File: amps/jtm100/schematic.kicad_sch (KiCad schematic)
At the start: 82 parts, among them T1 OT

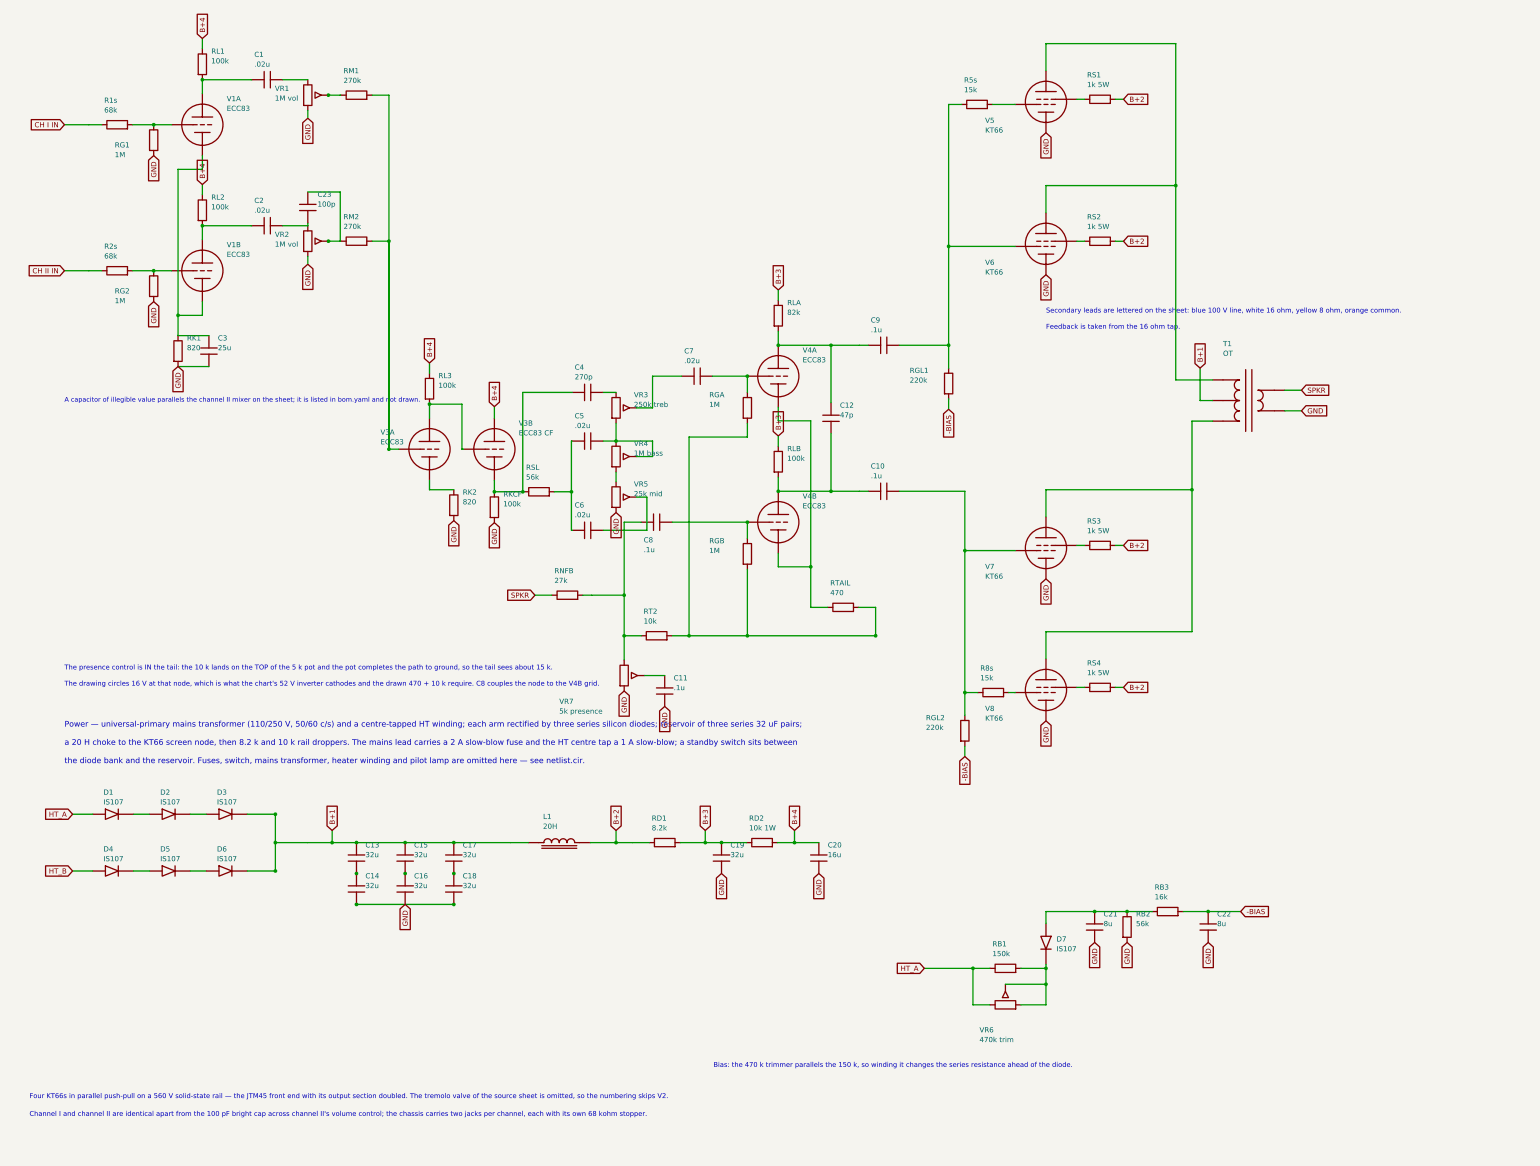
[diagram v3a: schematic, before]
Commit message: Fix: deterministic schematic ids and wires split at every join
- _u() is uuid5 over (amp id, emission order), so a regeneration of an
  unchanged script is byte-identical and a drift gate becomes possible
- write() splits wire segments at symbol pins, wire ends and junction dots,
  so the file connects exactly what the drawing shows under KiCad's
  endpoint-only semantics (270 pins were on a wire's interior; net
  partitions unchanged on all 38 sheets)
- all sheets regenerated; aa864-bassman title block was stale (draft) and
  now matches meta.yaml (verified)

Co-Authored-By: Claude Fable 5.1 <noreply@anthropic.com>
Claude-Session: https://claude.ai/code/session_01KBMfdh37HmCL2iWcBiL5J1
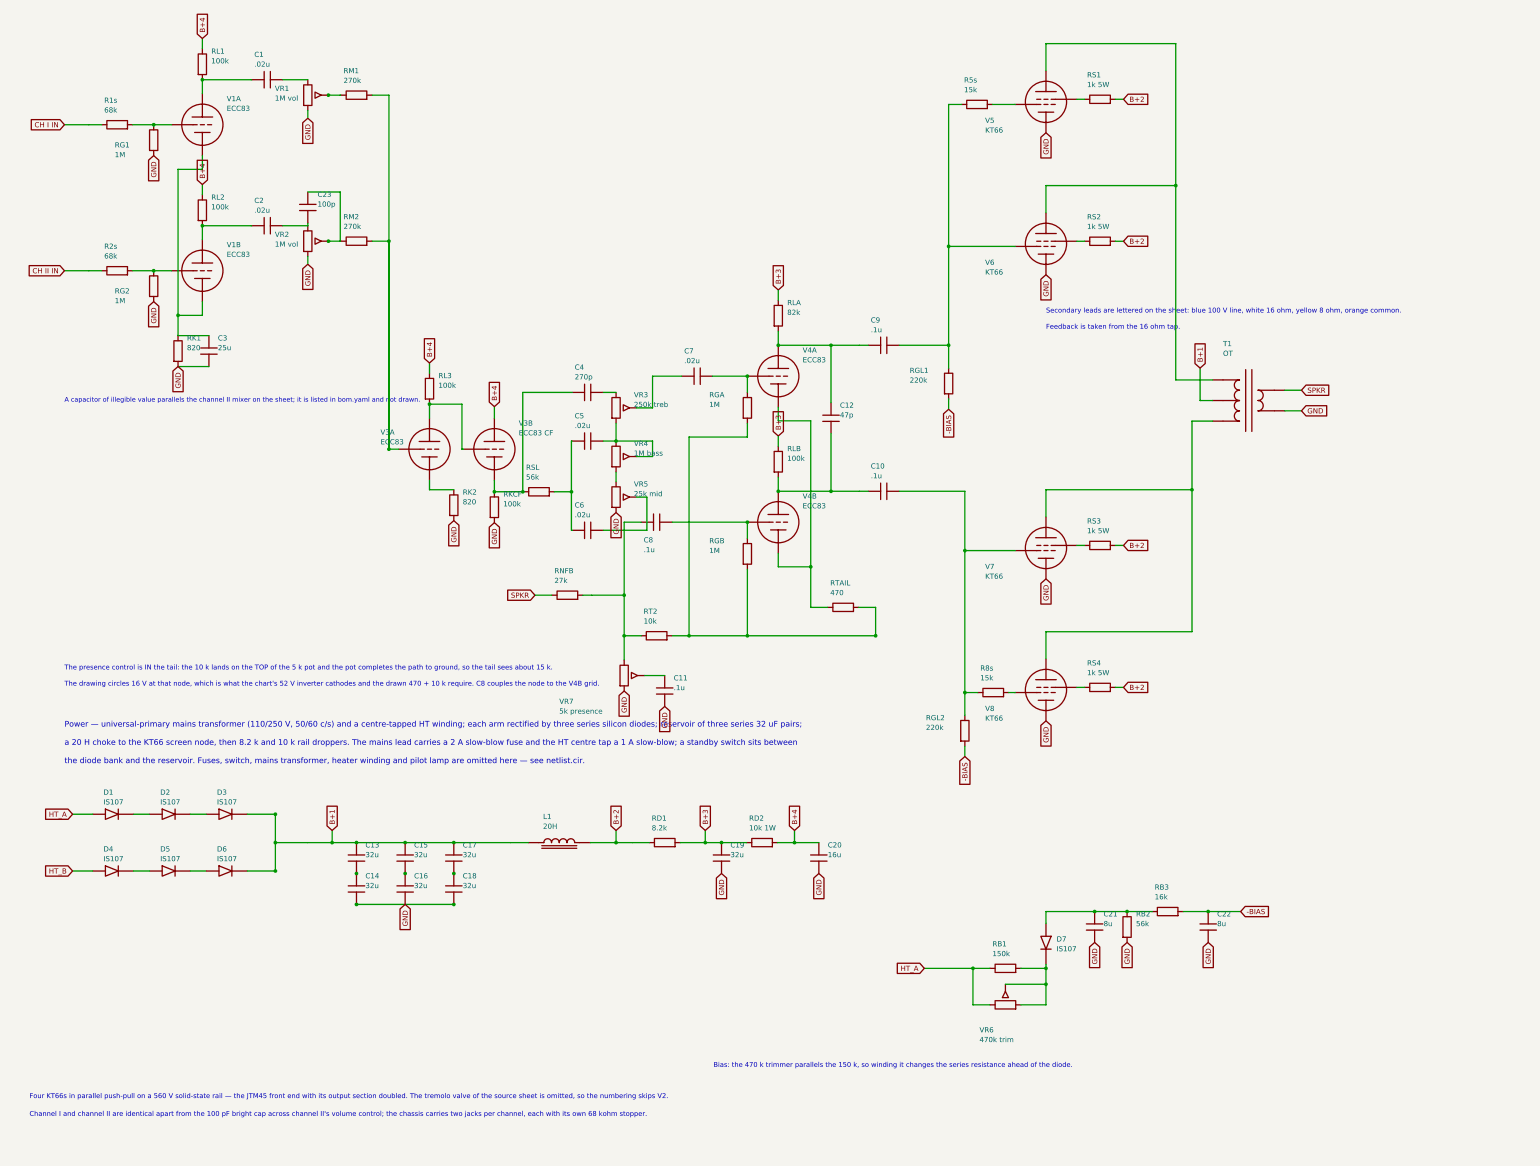
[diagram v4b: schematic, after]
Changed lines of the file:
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@@
   (wire (pts (xy 27.336 38.278) (xy 30.526 38.278))
     (stroke (width 0) (type default)))
-  (wire (pts (xy 38.146 38.278) (xy 47.716 38.278))
+  (wire (pts (xy 38.146 38.278) (xy 43.336 38.278))
+    (stroke (width 0) (type default)))
+  (wire (pts (xy 43.336 38.278) (xy 47.716 38.278))
     (stroke (width 0) (type default)))
   (junction (at 43.336 38.278) (diameter 0) (color 0 0 0 0))
@@
   (wire (pts (xy 97.146 30.988) (xy 101.336 30.988))
     (stroke (width 0) (type default)))
-  (wire (pts (xy 101.336 30.988) (xy 101.336 118.278))
+  (wire (pts (xy 101.336 30.988) (xy 101.336 66.988))
+    (stroke (width 0) (type default)))
+  (wire (pts (xy 101.336 66.988) (xy 101.336 118.278))
     (stroke (width 0) (type default)))
   (symbol (lib_id "cx:TRIODE") (at 55.336 74.278 0) (unit 1)
@@
   (wire (pts (xy 27.336 74.278) (xy 30.526 74.278))
     (stroke (width 0) (type default)))
-  (wire (pts (xy 38.146 74.278) (xy 47.716 74.278))
+  (wire (pts (xy 38.146 74.278) (xy 43.336 74.278))
+    (stroke (width 0) (type default)))
+  (wire (pts (xy 43.336 74.278) (xy 47.716 74.278))
     (stroke (width 0) (type default)))
   (junction (at 43.336 74.278) (diameter 0) (color 0 0 0 0))
@@
   (wire (pts (xy 55.336 49.278) (xy 49.336 49.278))
     (stroke (width 0) (type default)))
-  (wire (pts (xy 49.336 49.278) (xy 49.336 90.278))
+  (wire (pts (xy 49.336 49.278) (xy 49.336 85.278))
+    (stroke (width 0) (type default)))
+  (wire (pts (xy 49.336 85.278) (xy 49.336 90.278))
     (stroke (width 0) (type default)))
   (wire (pts (xy 55.336 81.898) (xy 55.336 85.278))
@@
   (wire (pts (xy 197.336 147.278) (xy 205.336 147.278))
     (stroke (width 0) (type default)))
-  (wire (pts (xy 205.336 111.278) (xy 205.336 157.278))
+  (wire (pts (xy 205.336 111.278) (xy 205.336 147.278))
+    (stroke (width 0) (type default)))
+  (wire (pts (xy 205.336 147.278) (xy 205.336 157.278))
     (stroke (width 0) (type default)))
   (junction (at 205.336 147.278) (diameter 0) (color 0 0 0 0))
@@
   (wire (pts (xy 163.526 136.278) (xy 159.336 136.278))
     (stroke (width 0) (type default)))
-  (wire (pts (xy 159.336 136.278) (xy 159.336 170.278))
+  (wire (pts (xy 159.336 136.278) (xy 159.336 154.278))
+    (stroke (width 0) (type default)))
+  (wire (pts (xy 159.336 154.278) (xy 159.336 164.278))
+    (stroke (width 0) (type default)))
+  (wire (pts (xy 159.336 164.278) (xy 159.336 170.278))
     (stroke (width 0) (type default)))
   (junction (at 159.336 164.278) (diameter 0) (color 0 0 0 0))
@@
   (wire (pts (xy 227.146 92.658) (xy 239.336 92.658))
     (stroke (width 0) (type default)))
-  (wire (pts (xy 239.336 33.278) (xy 239.336 92.658))
+  (wire (pts (xy 239.336 33.278) (xy 239.336 68.278))
+    (stroke (width 0) (type default)))
+  (wire (pts (xy 239.336 68.278) (xy 239.336 92.658))
     (stroke (width 0) (type default)))
   (junction (at 239.336 68.278) (diameter 0) (color 0 0 0 0))
@@
   (wire (pts (xy 227.146 128.658) (xy 243.336 128.658))
     (stroke (width 0) (type default)))
-  (wire (pts (xy 243.336 128.658) (xy 243.336 178.278))
+  (wire (pts (xy 243.336 128.658) (xy 243.336 143.278))
+    (stroke (width 0) (type default)))
+  (wire (pts (xy 243.336 143.278) (xy 243.336 178.278))
     (stroke (width 0) (type default)))
   (junction (at 243.336 143.278) (diameter 0) (color 0 0 0 0))
@@
   (wire (pts (xy 263.336 18.278) (xy 295.336 18.278))
     (stroke (width 0) (type default)))
-  (wire (pts (xy 295.336 18.278) (xy 295.336 101.198))
+  (wire (pts (xy 295.336 18.278) (xy 295.336 53.278))
+    (stroke (width 0) (type default)))
+  (wire (pts (xy 295.336 53.278) (xy 295.336 101.198))
     (stroke (width 0) (type default)))
   (wire (pts (xy 263.336 60.023) (xy 263.336 53.278))
@@
   (wire (pts (xy 263.336 163.278) (xy 299.336 163.278))
     (stroke (width 0) (type default)))
-  (wire (pts (xy 299.336 163.278) (xy 299.336 111.358))
+  (wire (pts (xy 299.336 163.278) (xy 299.336 128.278))
+    (stroke (width 0) (type default)))
+  (wire (pts (xy 299.336 128.278) (xy 299.336 111.358))
     (stroke (width 0) (type default)))
   (junction (at 299.336 128.278) (diameter 0) (color 0 0 0 0))
@@
     (stroke (width 0) (type default)))
   (junction (at 73.336 222.278) (diameter 0) (color 0 0 0 0))
-  (wire (pts (xy 73.336 208.278) (xy 73.336 222.278))
+  (wire (pts (xy 73.336 208.278) (xy 73.336 215.278))
+    (stroke (width 0) (type default)))
+  (wire (pts (xy 73.336 215.278) (xy 73.336 222.278))
     (stroke (width 0) (type default)))
   (wire (pts (xy 73.336 215.278) (xy 81.336 215.278))
@@
   (junction (at 117.336 215.278) (diameter 0) (color 0 0 0 0))
   (junction (at 117.336 222.898) (diameter 0) (color 0 0 0 0))
-  (wire (pts (xy 93.336 230.518) (xy 117.336 230.518))
+  (wire (pts (xy 93.336 230.518) (xy 105.336 230.518))
+    (stroke (width 0) (type default)))
+  (wire (pts (xy 105.336 230.518) (xy 117.336 230.518))
     (stroke (width 0) (type default)))
   (junction (at 93.336 230.518) (diameter 0) (color 0 0 0 0))
@@
   (global_label "GND" (shape input) (at 105.336 230.518 270)
     (effects (font (size 1.27 1.27)) (justify right)))
-  (wire (pts (xy 81.336 215.278) (xy 131.336 215.278))
+  (wire (pts (xy 81.336 215.278) (xy 87.336 215.278))
+    (stroke (width 0) (type default)))
+  (wire (pts (xy 87.336 215.278) (xy 93.336 215.278))
+    (stroke (width 0) (type default)))
+  (wire (pts (xy 93.336 215.278) (xy 105.336 215.278))
+    (stroke (width 0) (type default)))
+  (wire (pts (xy 105.336 215.278) (xy 117.336 215.278))
+    (stroke (width 0) (type default)))
+  (wire (pts (xy 117.336 215.278) (xy 131.336 215.278))
     (stroke (width 0) (type default)))
   (junction (at 87.336 215.278) (diameter 0) (color 0 0 0 0))
@@
     (property "Reference" "L1" (at 139.336 208.878 0) (effects (font (size 1.27 1.27)) (justify left)))
     (property "Value" "20H" (at 139.336 211.278 0) (effects (font (size 1.27 1.27)) (justify left))))
-  (wire (pts (xy 150.956 215.278) (xy 161.336 215.278))
+  (wire (pts (xy 150.956 215.278) (xy 157.336 215.278))
+    (stroke (width 0) (type default)))
+  (wire (pts (xy 157.336 215.278) (xy 161.336 215.278))
     (stroke (width 0) (type default)))
   (junction (at 157.336 215.278) (diameter 0) (color 0 0 0 0))
@@
   (wire (pts (xy 161.336 215.278) (xy 165.526 215.278))
     (stroke (width 0) (type default)))
-  (wire (pts (xy 173.146 215.278) (xy 183.336 215.278))
+  (wire (pts (xy 173.146 215.278) (xy 179.336 215.278))
+    (stroke (width 0) (type default)))
+  (wire (pts (xy 179.336 215.278) (xy 183.336 215.278))
     (stroke (width 0) (type default)))
   (junction (at 179.336 215.278) (diameter 0) (color 0 0 0 0))
@@
   (wire (pts (xy 183.336 215.278) (xy 189.526 215.278))
     (stroke (width 0) (type default)))
-  (wire (pts (xy 197.146 215.278) (xy 207.336 215.278))
+  (wire (pts (xy 197.146 215.278) (xy 201.336 215.278))
+    (stroke (width 0) (type default)))
+  (wire (pts (xy 201.336 215.278) (xy 207.336 215.278))
     (stroke (width 0) (type default)))
   (junction (at 201.336 215.278) (diameter 0) (color 0 0 0 0))
@@
   (wire (pts (xy 257.146 255.278) (xy 263.336 255.278))
     (stroke (width 0) (type default)))
-  (wire (pts (xy 263.336 255.278) (xy 263.336 246.278))
+  (wire (pts (xy 263.336 255.278) (xy 263.336 250.198))
+    (stroke (width 0) (type default)))
+  (wire (pts (xy 263.336 250.198) (xy 263.336 246.278))
     (stroke (width 0) (type default)))
   (junction (at 263.336 246.278) (diameter 0) (color 0 0 0 0))
@@
   (wire (pts (xy 263.336 235.198) (xy 263.336 232.278))
     (stroke (width 0) (type default)))
-  (wire (pts (xy 263.336 232.278) (xy 289.526 232.278))
+  (wire (pts (xy 263.336 232.278) (xy 275.336 232.278))
+    (stroke (width 0) (type default)))
+  (wire (pts (xy 275.336 232.278) (xy 283.336 232.278))
+    (stroke (width 0) (type default)))
+  (wire (pts (xy 283.336 232.278) (xy 289.526 232.278))
     (stroke (width 0) (type default)))
   (junction (at 275.336 232.278) (diameter 0) (color 0 0 0 0))

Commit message: Add: real tube pin numbers and readable valve glyphs on every schematic
Phase B of the drawing program. A factory service sheet numbers every tube
pin, because the number is what a technician puts a probe on. This corpus
printed none, and the numbers hidden in its symbols were positional
placeholders (P=1, G=2, K=3) that would have published a 6V6GT's plate as
pin 1 when it is pin 3.

1055 electrodes now carry the real number, 1027 lettered (27 are shared
filaments deduped, 1 dropped for want of clear space on the 6G2). Resolved per
instance from reference/tubes/<slug>.yaml through the same alias resolution the
layout renderer uses, so a 12AX7 section and a 6SL7 section each get their own
basing. A valve whose basing the corpus does not carry prints nothing rather
than a wrong number.

Section letters and basing units are now separate things, which cost a detour
worth recording. The RCA 12AX7-A sheet reads "Pin 1 - Plate of Unit No.2 ...
Pin 6 - Plate of Unit No.1", so unit numbering is not pin order; the 5Y3 and
GZ34 number their units in opposite pin order, so nothing positional can
express it. But the section LETTER is a designator, not a basing fact: this
corpus, like every technician, calls the first stage in signal order V1A, and
five amps' prose already did. On four amps the factory sheets put that first
stage on the other half -- the AA764's own schematic prints +200 V on pin 1 --
so those drawings now state their unit explicitly, each citing its source, and
no letter, netlist, parts list or layout comment changed. 183 layout comments
agree with the printed numbers, 0 disagree. A guard fires if two halves of one
bottle resolve to the same unit, which is exactly how this was found.

Glyphs: the cathode gains a bracket and filament hairpin so it can no longer be
confused with the plate bar, the pentode's screen sits on its own row, and a
rectifier draws as one envelope over its sections instead of two apparent
bottles. Line weights are scaled per sheet to a co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
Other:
- note added: "1"
- note added: "2"
- note added: "3"
- note added: "4"
- note added: "5"
- note added: "6"
- note added: "7"
- note added: "8"
